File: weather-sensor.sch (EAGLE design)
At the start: 31 parts, among them J1 43841-0005, J2 95501-6889, U1 SHT31, U2 MPL3115A2LGA8, U3 P82B715SOIC, U4 ADC081C021SOT-DDC, U5 MIC5219-3.3YM5-TR

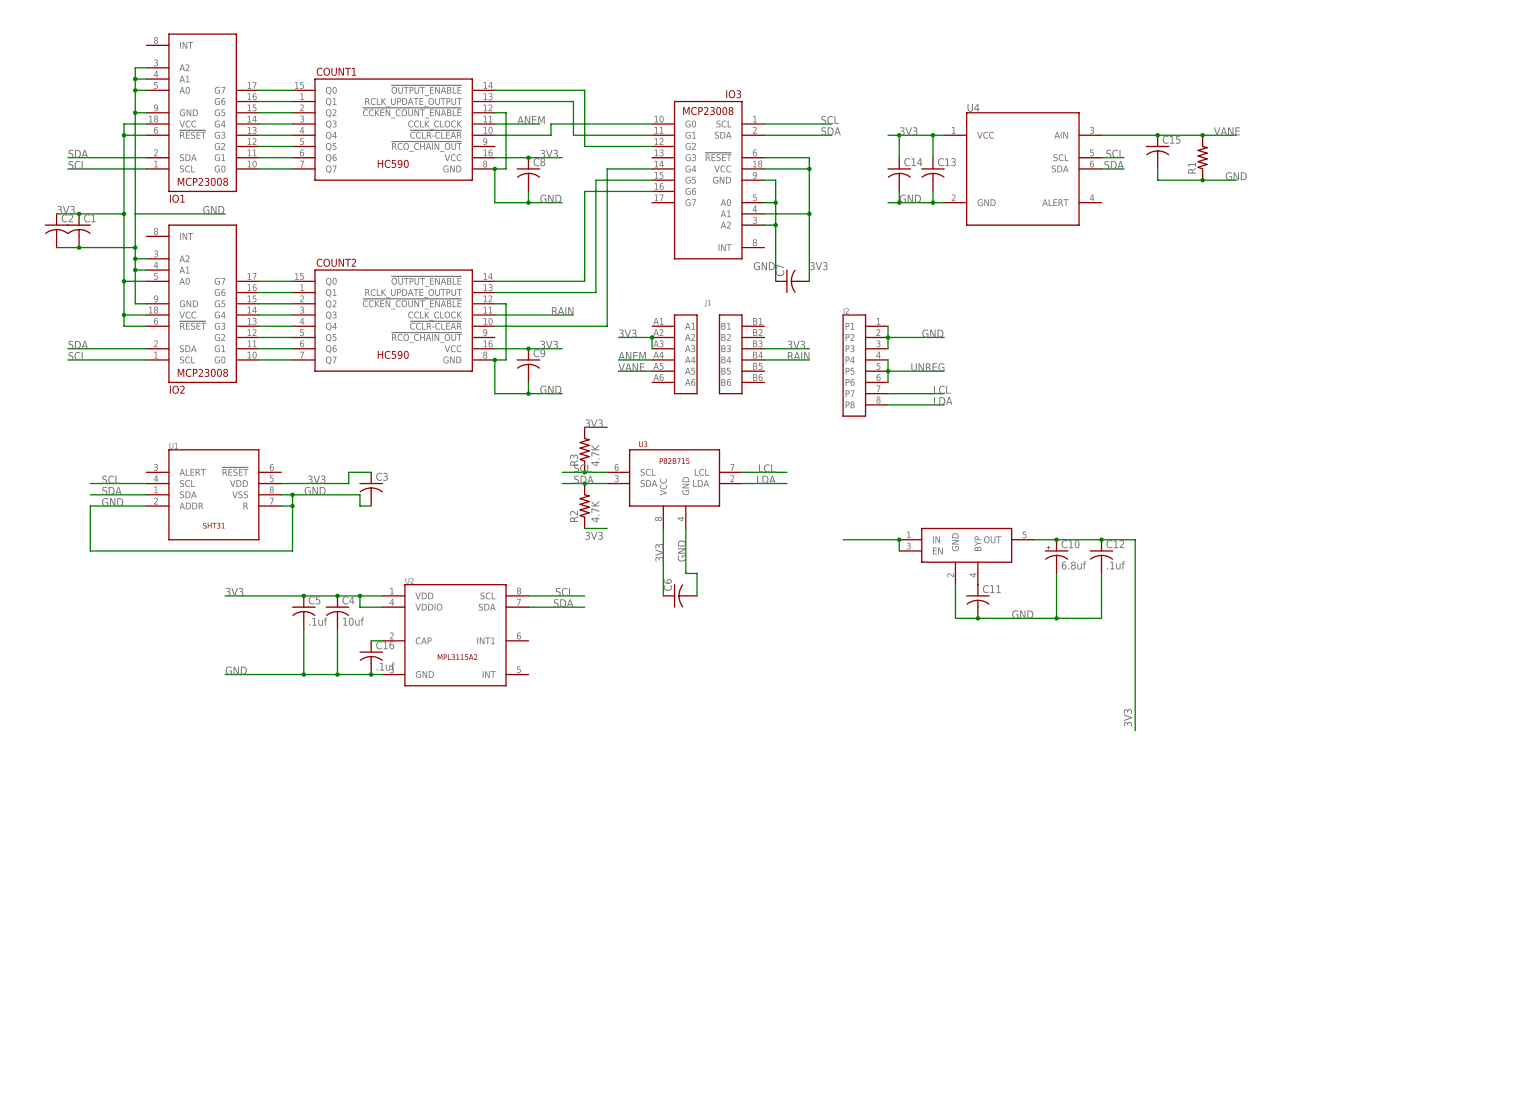
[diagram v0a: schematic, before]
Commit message: Changed range extender and added debounce to switched inputs.
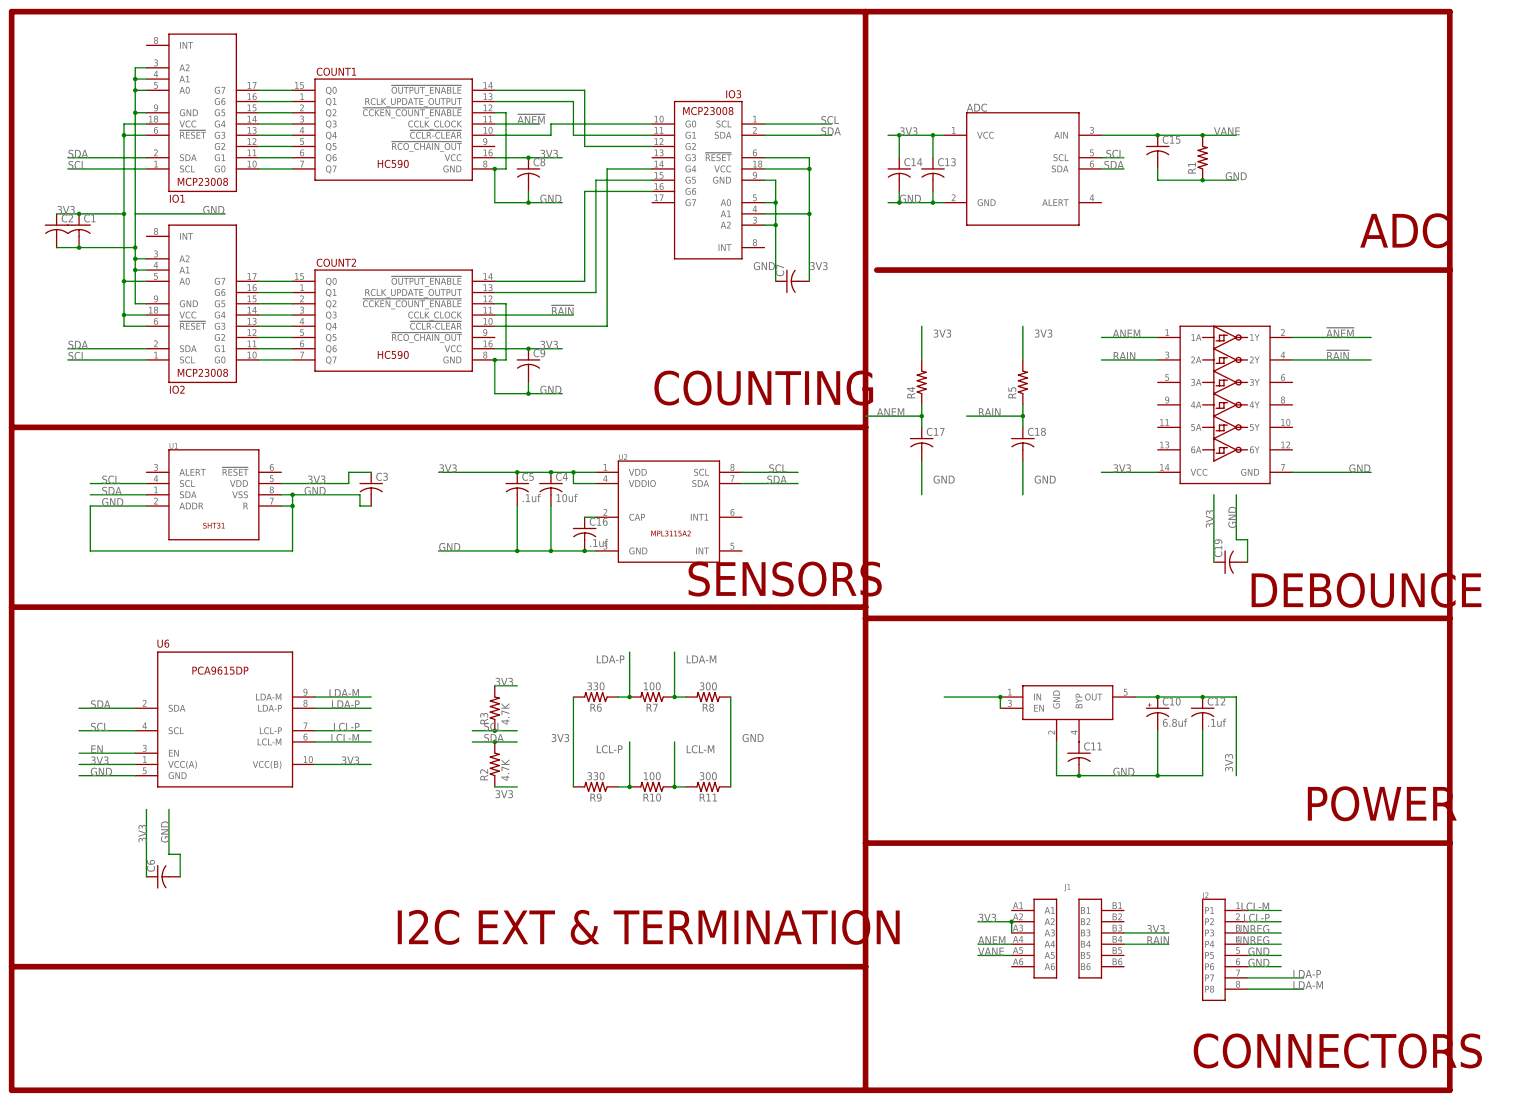
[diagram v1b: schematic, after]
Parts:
- removed U3: P82B715SOIC, Conservify:P82B715SOIC
- added C17, C18, C19: (no value), rcl:C-USC0603K
- added INVERTER: 74HC14, Conservify:74HC14
- added R10, R7: 100, SparkFun-Resistors:100KOHM-0603-1/10W-1%
- added R11, R8: 300, SparkFun-Resistors:100KOHM-0603-1/10W-1%
- added R4, R5: (no value), rcl:R-US_R0603
- added R6, R9: 330, SparkFun-Resistors:100KOHM-0603-1/10W-1%
- added U6: PCA9615, Conservify:PCA9615
- renumbered U4 to ADC
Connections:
- removed net LCL: J2.P7, U3.LCL
- removed net LDA: J2.P8, U3.LDA
- new net !ANEM: COUNT1.CCLK_CLOCK, INVERTER.1Y
- new net !RAIN: COUNT2.CCLK_CLOCK, INVERTER.2Y
- new net EN: U6.EN
- new net LCL-M: J2.P1, R10.1, R11.2, U6.LCL-M
- new net LCL-P: J2.P2, R10.2, R9.1, U6.LCL-P
- new net LDA-M: J2.P8, R7.1, R8.2, U6.LDA-M
- new net LDA-P: J2.P7, R6.1, R7.2, U6.LDA-P
- net 3V3: now also C19.1, INVERTER.VCC, R4.2, R5.2, R6.2, R9.2, U6.VCC(A), U6.VCC(B); no longer U3.VCC
- net ANEM: now also C17.1, INVERTER.1A, R4.1; no longer COUNT1.CCLK_CLOCK
- net GND: now also C17.2, C18.2, C19.2, INVERTER.GND, J2.P5, J2.P6, R11.1, R8.1, U6.GND; no longer J2.P1, J2.P2, J2.P3, U3.GND
- net RAIN: now also C18.1, INVERTER.2A, R5.1; no longer COUNT2.CCLK_CLOCK
- net SCL: now also U6.SCL; no longer U3.SCL
- net SDA: now also U6.SDA; no longer U3.SDA
- net UNREG: now also J2.P3; no longer J2.P5, J2.P6
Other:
- note added: "ADC"
- note added: "CONNECTORS"
- note added: "COUNTING"
- note added: "DEBOUNCE"
- note added: "I2C EXT & TERMINATION"
- note added: "POWER"
- note added: "SENSORS"
- moved on the sheet: C10, C11, C12, C16, C4, C5, C6, J1, J2, R2, R3, U2

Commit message: Changed power architecture for module/sesnor power synchronization. TA4.
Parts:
- added FID1, FID2, FID3, FID4: FIDUCIAL1X2.5, microbuilder:FIDUCIAL1X2.5
- C13: value (none) -> .1u
- C14: value (none) -> 4.7u
- C15: value (none) -> 470p
- C17, C18: value (none) -> 1uf
- R1, R4, R5: value (none) -> 10k
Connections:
- net N$11 renamed 2OE
- net N$21 renamed 2RCLK
- net N$22 renamed 2CCLR
- new net ENABLE: J2.P3, U5.EN
- net 3V3: now also IO1.A2; no longer J1.A3, J1.B3
- net GND: now also J1.A3, J1.B3; no longer IO1.A2
- net UNREG: no longer J2.P3, U5.EN
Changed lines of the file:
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@@
 <?xml version="1.0" encoding="utf-8"?>
 <!DOCTYPE eagle SYSTEM "eagle.dtd">
-<eagle version="9.4.2">
+<eagle version="9.5.0">
 <drawing>
 <settings>
@@
 <part name="C12" library="rcl" library_urn="urn:adsk.eagle:library:334" deviceset="C-US" device="C0603K" package3d_urn="urn:adsk.eagle:package:23680/2" value=".1uf"/>
 <part name="ADC" library="Conservify" library_urn="urn:adsk.eagle:library:11839183" deviceset="ADC081C021" device="SOT-DDC" package3d_urn="urn:adsk.eagle:package:11899194/1"/>
-<part name="C13" library="rcl" library_urn="urn:adsk.eagle:library:334" deviceset="C-US" device="C0603K" package3d_urn="urn:adsk.eagle:package:23680/2"/>
-<part name="C14" library="rcl" library_urn="urn:adsk.eagle:library:334" deviceset="C-US" device="C0603K" package3d_urn="urn:adsk.eagle:package:23680/2"/>
-<part name="C15" library="rcl" library_urn="urn:adsk.eagle:library:334" deviceset="C-US" device="C0603K" package3d_urn="urn:adsk.eagle:package:23680/2"/>
-<part name="R1" library="rcl" library_urn="urn:adsk.eagle:library:334" deviceset="R-US_" device="R0603" package3d_urn="urn:adsk.eagle:package:23555/3"/>
+<part name="C13" library="rcl" library_urn="urn:adsk.eagle:library:334" deviceset="C-US" device="C0603K" package3d_urn="urn:adsk.eagle:package:23680/2" value=".1u"/>
+<part name="C14" library="rcl" library_urn="urn:adsk.eagle:library:334" deviceset="C-US" device="C0603K" package3d_urn="urn:adsk.eagle:package:23680/2" value="4.7u"/>
+<part name="C15" library="rcl" library_urn="urn:adsk.eagle:library:334" deviceset="C-US" device="C0603K" package3d_urn="urn:adsk.eagle:package:23680/2" value="470p"/>
+<part name="R1" library="rcl" library_urn="urn:adsk.eagle:library:334" deviceset="R-US_" device="R0603" package3d_urn="urn:adsk.eagle:package:23555/3" value="10k"/>
 <part name="C16" library="rcl" library_urn="urn:adsk.eagle:library:334" deviceset="C-US" device="C0603K" package3d_urn="urn:adsk.eagle:package:23680/2" value=".1uf"/>
 <part name="R2" library="rcl" library_urn="urn:adsk.eagle:library:334" deviceset="R-US_" device="R0603" package3d_urn="urn:adsk.eagle:package:23555/3" value="4.7K"/>
 <part name="R3" library="rcl" library_urn="urn:adsk.eagle:library:334" deviceset="R-US_" device="R0603" package3d_urn="urn:adsk.eagle:package:23555/3" value="4.7K"/>
-<part name="R4" library="rcl" library_urn="urn:adsk.eagle:library:334" deviceset="R-US_" device="R0603" package3d_urn="urn:adsk.eagle:package:23555/3"/>
-<part name="C17" library="rcl" library_urn="urn:adsk.eagle:library:334" deviceset="C-US" device="C0603K" package3d_urn="urn:adsk.eagle:package:23680/2"/>
-<part name="R5" library="rcl" library_urn="urn:adsk.eagle:library:334" deviceset="R-US_" device="R0603" package3d_urn="urn:adsk.eagle:package:23555/3"/>
-<part name="C18" library="rcl" library_urn="urn:adsk.eagle:library:334" deviceset="C-US" device="C0603K" package3d_urn="urn:adsk.eagle:package:23680/2"/>
+<part name="R4" library="rcl" library_urn="urn:adsk.eagle:library:334" deviceset="R-US_" device="R0603" package3d_urn="urn:adsk.eagle:package:23555/3" value="10k"/>
+<part name="C17" library="rcl" library_urn="urn:adsk.eagle:library:334" deviceset="C-US" device="C0603K" package3d_urn="urn:adsk.eagle:package:23680/2" value="1uf"/>
+<part name="R5" library="rcl" library_urn="urn:adsk.eagle:library:334" deviceset="R-US_" device="R0603" package3d_urn="urn:adsk.eagle:package:23555/3" value="10k"/>
+<part name="C18" library="rcl" library_urn="urn:adsk.eagle:library:334" deviceset="C-US" device="C0603K" package3d_urn="urn:adsk.eagle:package:23680/2" value="1uf"/>
 <part name="INVERTER" library="Conservify" library_urn="urn:adsk.eagle:library:11839183" deviceset="74HC14" device="" package3d_urn="urn:adsk.eagle:package:12729521/1"/>
 <part name="U6" library="Conservify" library_urn="urn:adsk.eagle:library:11839183" deviceset="PCA9615" device="" package3d_urn="urn:adsk.eagle:package:12823946/1"/>
@@
 <part name="R11" library="SparkFun-Resistors" library_urn="urn:adsk.eagle:library:532" deviceset="100KOHM" device="-0603-1/10W-1%" package3d_urn="urn:adsk.eagle:package:39650/1" value="300"/>
 <part name="C19" library="rcl" library_urn="urn:adsk.eagle:library:334" deviceset="C-US" device="C0603K" package3d_urn="urn:adsk.eagle:package:23680/2"/>
+<part name="FID1" library="microbuilder" deviceset="FIDUCIAL" device="1X2.5"/>
+<part name="FID2" library="microbuilder" deviceset="FIDUCIAL" device="1X2.5"/>
+<part name="FID3" library="microbuilder" deviceset="FIDUCIAL" device="1X2.5"/>
+<part name="FID4" library="microbuilder" deviceset="FIDUCIAL" device="1X2.5"/>
 </parts>
 <sheets>
@@
 <attribute name="VALUE" x="207.391" y="28.956" size="1.778" layer="96" rot="R90"/>
 </instance>
+<instance part="FID1" gate="G$1" x="-35.56" y="-78.74" smashed="yes"/>
+<instance part="FID2" gate="G$1" x="-25.4" y="-78.74" smashed="yes"/>
+<instance part="FID3" gate="G$1" x="-17.78" y="-78.74" smashed="yes"/>
+<instance part="FID4" gate="G$1" x="-7.62" y="-78.74" smashed="yes"/>
 </instances>
 <busses>
@@
 <pinref part="J1" gate="G$1" pin="A2"/>
 <wire x1="154.94" y1="-53.34" x2="147.32" y2="-53.34" width="0.1524" layer="91"/>
-<pinref part="J1" gate="G$1" pin="A3"/>
-<wire x1="154.94" y1="-55.88" x2="154.94" y2="-53.34" width="0.1524" layer="91"/>
-<junction x="154.94" y="-53.34"/>
 <label x="147.32" y="-53.34" size="1.778" layer="95"/>
-</segment>
-<segment>
-<pinref part="J1" gate="G$1" pin="B3"/>
-<wire x1="180.34" y1="-55.88" x2="190.5" y2="-55.88" width="0.1524" layer="91"/>
-<label x="185.42" y="-55.88" size="1.778" layer="95"/>
 </segment>
 <segment>
@@
 <label x="200.66" y="35.56" size="1.778" layer="95" rot="R90"/>
 <pinref part="C19" gate="G$1" pin="1"/>
+</segment>
+<segment>
+<pinref part="IO1" gate="G$1" pin="A2"/>
+<wire x1="-40.64" y1="139.7" x2="-48.26" y2="139.7" width="0.1524" layer="91"/>
+<label x="-48.26" y="139.7" size="1.778" layer="95"/>
 </segment>
 </net>
@@
 <pinref part="IO1" gate="G$1" pin="A1"/>
 <wire x1="-43.18" y1="137.16" x2="-40.64" y2="137.16" width="0.1524" layer="91"/>
-<pinref part="IO1" gate="G$1" pin="A2"/>
-<wire x1="-40.64" y1="139.7" x2="-43.18" y2="139.7" width="0.1524" layer="91"/>
-<wire x1="-43.18" y1="139.7" x2="-43.18" y2="137.16" width="0.1524" layer="91"/>
-<junction x="-43.18" y="137.16"/>
 <wire x1="-43.18" y1="134.62" x2="-43.18" y2="129.54" width="0.1524" layer="91"/>
 <junction x="-43.18" y="134.62"/>
@@
 <wire x1="208.28" y1="33.02" x2="208.28" y2="27.94" width="0.1524" layer="91"/>
 </segment>
+<segment>
+<pinref part="J1" gate="G$1" pin="A3"/>
+<wire x1="154.94" y1="-55.88" x2="147.32" y2="-55.88" width="0.1524" layer="91"/>
+<label x="147.32" y="-55.88" size="1.778" layer="95"/>
+</segment>
+<segment>
+<pinref part="J1" gate="G$1" pin="B3"/>
+<wire x1="180.34" y1="-55.88" x2="190.5" y2="-55.88" width="0.1524" layer="91"/>
+<label x="185.42" y="-55.88" size="1.778" layer="95"/>
+</segment>
 </net>
 <net name="N$1" class="0">
@@
 </segment>
 </net>
-<net name="N$11" class="0">
+<net name="2OE" class="0">
 <segment>
 <pinref part="COUNT2" gate="G$1" pin="!OUTPUT_ENABLE"/>
@@
 <pinref part="IO3" gate="G$1" pin="G6"/>
 <wire x1="73.66" y1="111.76" x2="58.42" y2="111.76" width="0.1524" layer="91"/>
-</segment>
-</net>
-<net name="N$21" class="0">
+<label x="45.72" y="91.44" size="1.778" layer="95"/>
+</segment>
+</net>
+<net name="2RCLK" class="0">
 <segment>
 <pinref part="COUNT2" gate="G$1" pin="RCLK_UPDATE_OUTPUT"/>
@@
 <pinref part="IO3" gate="G$1" pin="G5"/>
 <wire x1="60.96" y1="114.3" x2="73.66" y2="114.3" width="0.1524" layer="91"/>
-</segment>
-</net>
-<net name="N$22" class="0">
+<label x="45.72" y="88.9" size="1.778" layer="95"/>
+</segment>
+</net>
+<net name="2CCLR" class="0">
 <segment>
 <pinref part="COUNT2" gate="G$1" pin="!CCLR-CLEAR"/>
@@
 <pinref part="IO3" gate="G$1" pin="G4"/>
 <wire x1="73.66" y1="116.84" x2="63.5" y2="116.84" width="0.1524" layer="91"/>
+<label x="45.72" y="81.28" size="1.778" layer="95"/>
 </segment>
 </net>
@@
 <pinref part="U5" gate="G$1" pin="IN"/>
 <wire x1="152.4" y1="-2.54" x2="139.7" y2="-2.54" width="0.1524" layer="91"/>
-<pinref part="U5" gate="G$1" pin="EN"/>
-<wire x1="152.4" y1="-5.08" x2="152.4" y2="-2.54" width="0.1524" layer="91"/>
-<junction x="152.4" y="-2.54"/>
-</segment>
-<segment>
-<pinref part="J2" gate="G$1" pin="P3"/>
-<wire x1="208.28" y1="-55.88" x2="215.9" y2="-55.88" width="0.1524" layer="91"/>
-<label x="213.36" y="-55.88" size="1.778" layer="95" align="bottom-right"/>
+<label x="142.24" y="-2.54" size="1.778" layer="95"/>
 </segment>
 <segment>
@@
 </segment>
 </net>
+<net name="ENABLE" class="0">
+<segment>
+<pinref part="J2" gate="G$1" pin="P3"/>
+<wire x1="208.28" y1="-55.88" x2="215.9" y2="-55.88" width="0.1524" layer="91"/>
+<label x="213.36" y="-55.88" size="1.778" layer="95" align="bottom-right"/>
+</segment>
+<segment>
+<pinref part="U5" gate="G$1" pin="EN"/>
+<wire x1="152.4" y1="-5.08" x2="139.7" y2="-5.08" width="0.1524" layer="91"/>
+<label x="142.24" y="-5.08" size="1.778" layer="95"/>
+</segment>
+</net>
